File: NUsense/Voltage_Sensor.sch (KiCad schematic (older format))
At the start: 4 parts, among them U11? ACS724

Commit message: Change hierarchy layout
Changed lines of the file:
@@
 LIBS:valves
 LIBS:ADM6713RAKS
+LIBS:Header_Connectors
 LIBS:MPU6000
 LIBS:NUbots
 LIBS:STM32F746ZGT6
-LIBS:Header_Connectors
 LIBS:NUsense-cache
 EELAYER 25 0
@@
 Connection ~ 3750 1600
 Connection ~ 3450 1700
-Text GLabel 4150 1700 2    60   Input ~ 0
+Text HLabel 4150 1700 2    60   Output ~ 0
 I_OUT
 $EndSCHEMATC

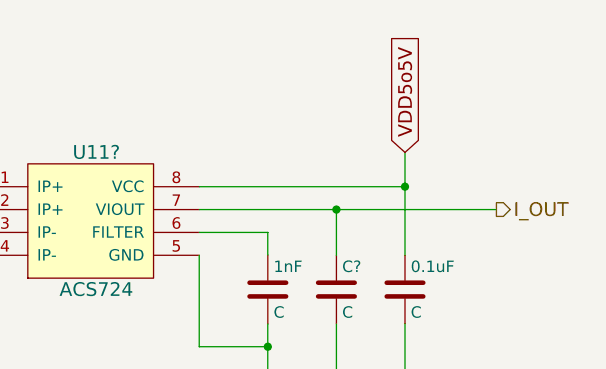
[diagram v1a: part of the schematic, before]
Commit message: Add power components
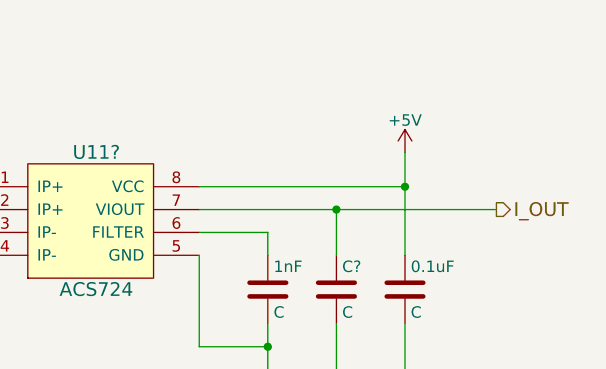
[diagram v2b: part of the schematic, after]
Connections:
- net VDD5o5V renamed +5V
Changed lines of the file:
@@
 	1600 1600 1900 1600
 Connection ~ 1800 1600
-Text GLabel 3750 1450 1    60   Input ~ 0
-VDD5o5V
 Connection ~ 3750 1600
 Connection ~ 3450 1700
 Text HLabel 4150 1700 2    60   Output ~ 0
 I_OUT
+$Comp
+L +5V #PWR?
+U 1 1 5A71C782
+P 3750 1450
+F 0 "#PWR?" H 3750 1300 50  0001 C CNN
+F 1 "+5V" H 3750 1590 50  0000 C CNN
+F 2 "" H 3750 1450 50  0001 C CNN
+F 3 "" H 3750 1450 50  0001 C CNN
+	1    3750 1450
+	1    0    0    -1
+$EndComp
 $EndSCHEMATC

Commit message: Correct Broken Files
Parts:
- added C? (x9): C, symbol C
- added R? (x7): R, symbol R
- added R?: R_Variable, symbol R_Variable
- added R?: 1M, symbol R
- added U?: bq76920, symbol bq76920
- added U?: 5_PIN_JST, symbol 5_PIN_JST
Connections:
- net GND: now also C?.2, C?.2, C?.2, C?.2, R?.1, R?.1, U?.3 (VSS)
- new net: C?.1, R?.1, U?.10 (BAT)
- new net: C?.1, C?.2, R?.1, R?.2, U?.12 (VC5), U?.9 (REGSRC)
- new net: C?.1, C?.2, R?.1, U?.13 (VC4), U?.14 (VC3)
- new net: C?.1, C?.2, R?.1, U?.15 (VC2)
- new net: C?.1, C?.2, R?.1, R?.1, U?.16 (VC1)
- new net: C?.1, R?.1, U?.17 (VC0)
- new net: R?.2, R?.2, U?.6 (TS1)
- new net: C?.1, U?.7 (CAP1)
- new net: C?.1, C?.2, R?.2, U?.1 (GND)
- new net: R?.2, U?.2 (V1)
- new net: R?.2, U?.3 (V2)
- new net: R?.2, U?.4 (V3)
- new net: R?.2, U?.5 (V4)
- new net +3V3: C?.1, U?.8 (REGOUT)
- new net VS_ALERT: R?.2, U?.20 (ALERT)
- new net VS_SCL: U?.5 (SCL)
- new net VS_SDA: U?.4 (SDA)

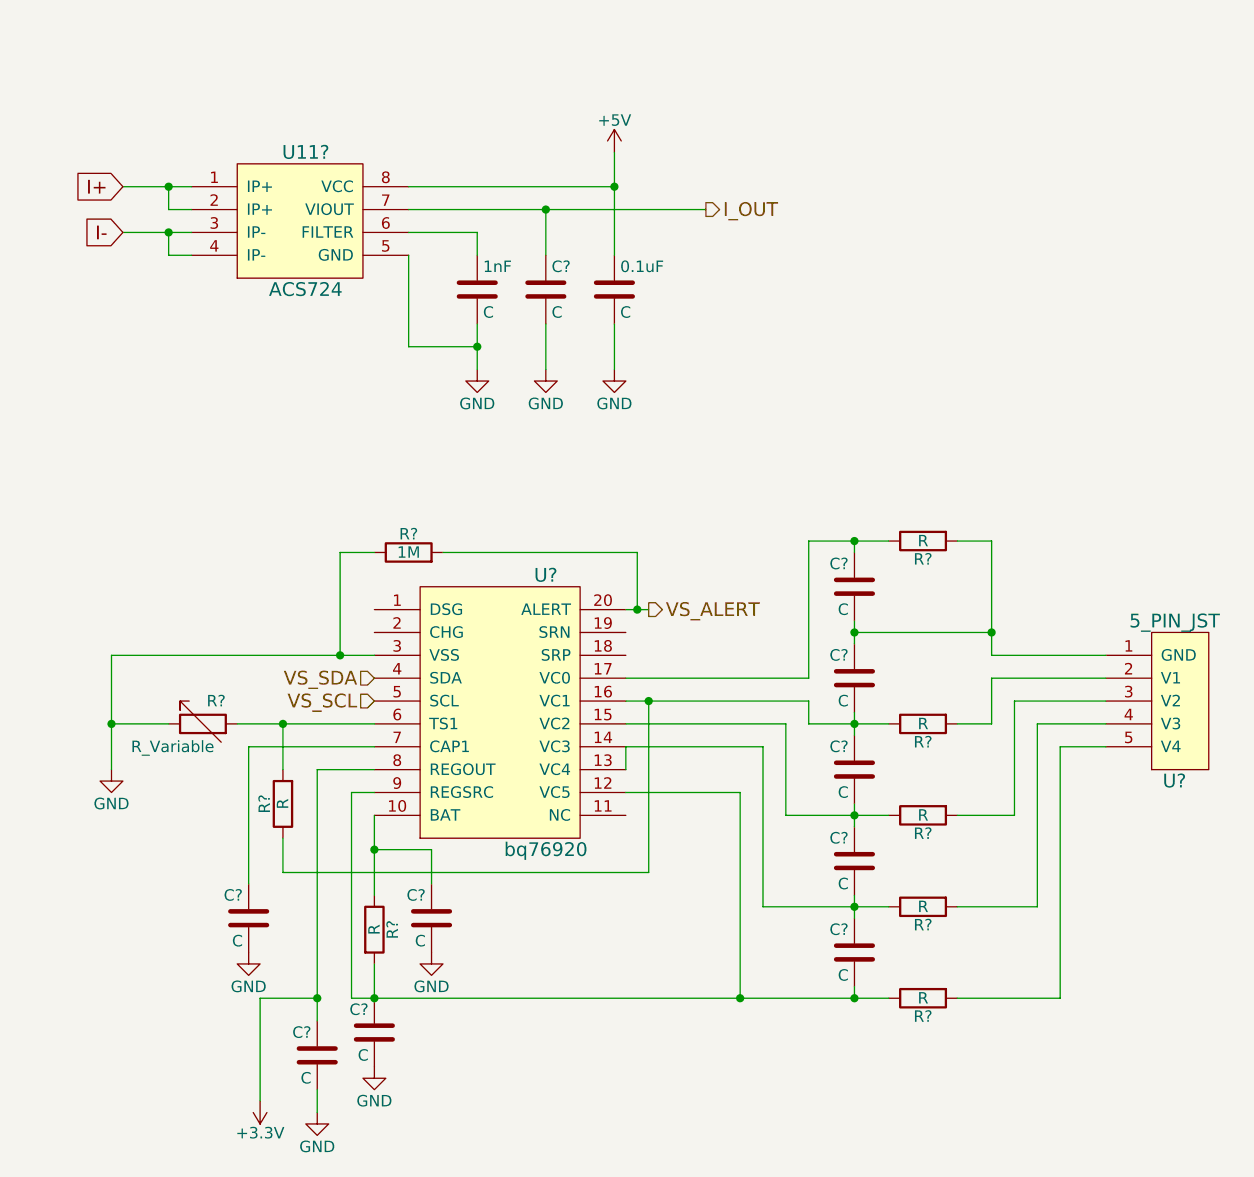
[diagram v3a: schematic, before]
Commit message: Adds annotations and footprints to all components
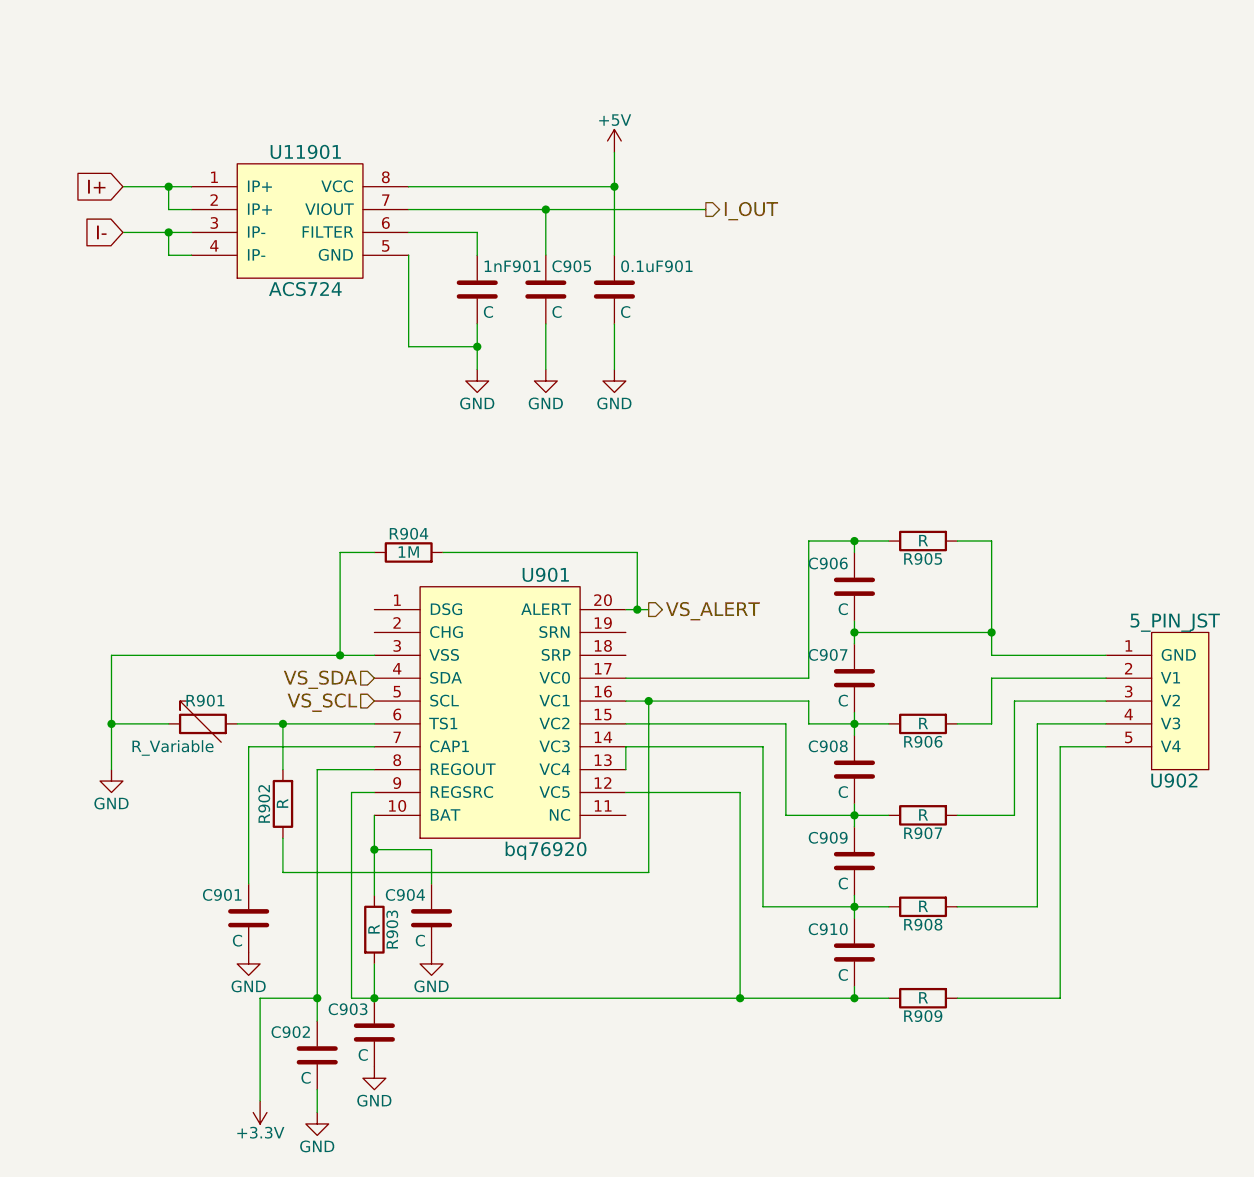
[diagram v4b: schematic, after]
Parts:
- 0.1uF901: renamed from 0.1uF; footprint (none) -> Capacitors_SMD:C_0805_HandSoldering
- 1nF901: renamed from 1nF; footprint (none) -> Capacitors_SMD:C_0805_HandSoldering
- C901, C902, C903, C904, C905, C906, C907, C908, C909, C910: renamed from C?; footprint (none) -> Capacitors_SMD:C_0805_HandSoldering
- R901, R902, R903, R904, R905, R906, R907, R908, R909: renamed from R?; footprint (none) -> Resistors_SMD:R_0805_HandSoldering
- U11901: renamed from U11?; footprint (none) -> Footprints:SOIC-8
- U901: renamed from U?; footprint (none) -> Footprints:SOIC-20
- gave numbers to parts that had none: 1

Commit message: More Changes
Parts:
- 0.1uF701: renamed from 0.1uF901; value C -> 0.1nF
- 1nF701: renamed from 1nF901; value C -> 1nF
- renumbered C901 to C701, C902 to C702, C903 to C703, C904 to C704, C905 to C705, C906 to C706, C907 to C707, C908 to C708, C909 to C709, C910 to C710, R901 to R701, R902 to R702, R903 to R703, R904 to R704, R905 to R705, R906 to R706, R907 to R707, R908 to R708, R909 to R709, U11901 to U701, U901 to U702, U902 to U703
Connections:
- net I+ renamed BATT_+
- net I- renamed BATT_-
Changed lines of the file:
@@
 $Descr A4 11693 8268
 encoding utf-8
-Sheet 9 12
+Sheet 7 12
 Title ""
 Date ""
@@
 $EndDescr
 $Comp
-L ACS724 U11901
+L ACS724 U701
 U 1 1 5A6D62FA
 P 2100 2000
-F 0 "U11901" H 2400 2550 60  0000 C CNN
+F 0 "U701" H 2400 2550 60  0000 C CNN
 F 1 "ACS724" H 2400 1950 60  0000 C CNN
 F 2 "Footprints:SOIC-8" H 2100 2000 60  0001 C CNN
@@
 $EndComp
 $Comp
-L C 1nF901
+L C 1nF701
 U 1 1 5A6D635A
 P 3150 2050
-F 0 "1nF901" H 3175 2150 50  0000 L CNN
-F 1 "C" H 3175 1950 50  0000 L CNN
+F 0 "1nF701" H 3175 2150 50  0000 L CNN
+F 1 "1nF" H 3175 1950 50  0000 L CNN
 F 2 "Capacitors_SMD:C_0805_HandSoldering" H 3188 1900 50  0001 C CNN
 F 3 "" H 3150 2050 50  0001 C CNN
@@
 $EndComp
 $Comp
-L C C905
+L C C705
 U 1 1 5A6D63B5
 P 3450 2050
-F 0 "C905" H 3475 2150 50  0000 L CNN
+F 0 "C705" H 3475 2150 50  0000 L CNN
 F 1 "C" H 3475 1950 50  0000 L CNN
 F 2 "Capacitors_SMD:C_0805_HandSoldering" H 3488 1900 50  0001 C CNN
@@
 $EndComp
 $Comp
-L C 0.1uF901
+L C 0.1uF701
 U 1 1 5A6D63DA
 P 3750 2050
-F 0 "0.1uF901" H 3775 2150 50  0000 L CNN
-F 1 "C" H 3775 1950 50  0000 L CNN
+F 0 "0.1uF701" H 3775 2150 50  0000 L CNN
+F 1 "0.1nF" H 3775 1950 50  0000 L CNN
 F 2 "Capacitors_SMD:C_0805_HandSoldering" H 3788 1900 50  0001 C CNN
 F 3 "" H 3750 2050 50  0001 C CNN
@@
 $EndComp
 $Comp
-L GND #PWR907
+L GND #PWR067
 U 1 1 5A6D644B
 P 3150 2400
-F 0 "#PWR907" H 3150 2150 50  0001 C CNN
+F 0 "#PWR067" H 3150 2150 50  0001 C CNN
 F 1 "GND" H 3150 2250 50  0000 C CNN
 F 2 "" H 3150 2400 50  0001 C CNN
@@
 $EndComp
 $Comp
-L GND #PWR908
+L GND #PWR068
 U 1 1 5A6D6469
 P 3450 2400
-F 0 "#PWR908" H 3450 2150 50  0001 C CNN
+F 0 "#PWR068" H 3450 2150 50  0001 C CNN
 F 1 "GND" H 3450 2250 50  0000 C CNN
 F 2 "" H 3450 2400 50  0001 C CNN
@@
 $EndComp
 $Comp
-L GND #PWR910
+L GND #PWR069
 U 1 1 5A6D6480
 P 3750 2400
-F 0 "#PWR910" H 3750 2150 50  0001 C CNN
+F 0 "#PWR069" H 3750 2150 50  0001 C CNN
 F 1 "GND" H 3750 2250 50  0000 C CNN
 F 2 "" H 3750 2400 50  0001 C CNN
@@
 	1    0    0    -1
 $EndComp
-Text GLabel 1600 1600 0    60   Input ~ 0
-I+
-Text GLabel 1600 1800 0    60   Input ~ 0
-I-
 Text HLabel 4150 1700 2    60   Output ~ 0
 I_OUT
 $Comp
-L +5V #PWR909
+L +5V #PWR070
 U 1 1 5A71C782
 P 3750 1450
-F 0 "#PWR909" H 3750 1300 50  0001 C CNN
+F 0 "#PWR070" H 3750 1300 50  0001 C CNN
 F 1 "+5V" H 3750 1590 50  0000 C CNN
 F 2 "" H 3750 1450 50  0001 C CNN
@@
 $EndComp
 $Comp
-L bq76920 U901
+L bq76920 U702
 U 1 1 5A7144DD
 P 2900 4450
-F 0 "U901" H 3450 5600 60  0000 C CNN
+F 0 "U702" H 3450 5600 60  0000 C CNN
 F 1 "bq76920" H 3450 4400 60  0000 C CNN
 F 2 "Footprints:SOIC-20" H 2900 4450 60  0001 C CNN
@@
 $EndComp
 $Comp
-L 5_PIN_JST U902
+L 5_PIN_JST U703
 U 1 1 5A71501A
 P 6350 3550
-F 0 "U902" H 6500 4200 60  0000 C CNN
+F 0 "U703" H 6500 4200 60  0000 C CNN
 F 1 "5_PIN_JST" H 6500 3500 60  0000 C CNN
 F 2 "" H 6350 3550 60  0001 C CNN
@@
 $EndComp
 $Comp
-L R R907
+L R R707
 U 1 1 5A7150F8
 P 5100 4350
-F 0 "R907" V 5180 4350 50  0000 C CNN
+F 0 "R707" V 5180 4350 50  0000 C CNN
 F 1 "R" V 5100 4350 50  0000 C CNN
 F 2 "Resistors_SMD:R_0805_HandSoldering" V 5030 4350 50  0001 C CNN
@@
 $EndComp
 $Comp
-L R R905
+L R R705
 U 1 1 5A71513F
 P 5100 3150
-F 0 "R905" V 5180 3150 50  0000 C CNN
+F 0 "R705" V 5180 3150 50  0000 C CNN
 F 1 "R" V 5100 3150 50  0000 C CNN
 F 2 "Resistors_SMD:R_0805_HandSoldering" V 5030 3150 50  0001 C CNN
@@
 $EndComp
 $Comp
-L R R906
+L R R706
 U 1 1 5A71518D
 P 5100 3950
-F 0 "R906" V 5180 3950 50  0000 C CNN
+F 0 "R706" V 5180 3950 50  0000 C CNN
 F 1 "R" V 5100 3950 50  0000 C CNN
 F 2 "Resistors_SMD:R_0805_HandSoldering" V 5030 3950 50  0001 C CNN
@@
 $EndComp
 $Comp
-L C C907
+L C C707
 U 1 1 5A71527F
 P 4800 3750
-F 0 "C907" H 4825 3850 50  0000 L CNN
+F 0 "C707" H 4825 3850 50  0000 L CNN
 F 1 "C" H 4825 3650 50  0000 L CNN
 F 2 "Capacitors_SMD:C_0805_HandSoldering" H 4838 3600 50  0001 C CNN
@@
 $EndComp
 $Comp
-L C C908
+L C C708
 U 1 1 5A715314
 P 4800 4150
-F 0 "C908" H 4825 4250 50  0000 L CNN
+F 0 "C708" H 4825 4250 50  0000 L CNN
 F 1 "C" H 4825 4050 50  0000 L CNN
 F 2 "Capacitors_SMD:C_0805_HandSoldering" H 4838 4000 50  0001 C CNN
@@
 $EndComp
 $Comp
-L R R908
+L R R708
 U 1 1 5A7153F1
 P 5100 4750
-F 0 "R908" V 5180 4750 50  0000 C CNN
+F 0 "R708" V 5180 4750 50  0000 C CNN
 F 1 "R" V 5100 4750 50  0000 C CNN
 F 2 "Resistors_SMD:R_0805_HandSoldering" V 5030 4750 50  0001 C CNN
@@
 $EndComp
 $Comp
-L C C909
+L C C709
 U 1 1 5A7153F7
 P 4800 4550
-F 0 "C909" H 4825 4650 50  0000 L CNN
+F 0 "C709" H 4825 4650 50  0000 L CNN
 F 1 "C" H 4825 4450 50  0000 L CNN
 F 2 "Capacitors_SMD:C_0805_HandSoldering" H 4838 4400 50  0001 C CNN
@@
 $EndComp
 $Comp
-L R R909
+L R R709
 U 1 1 5A715441
 P 5100 5150
-F 0 "R909" V 5180 5150 50  0000 C CNN
+F 0 "R709" V 5180 5150 50  0000 C CNN
 F 1 "R" V 5100 5150 50  0000 C CNN
 F 2 "Resistors_SMD:R_0805_HandSoldering" V 5030 5150 50  0001 C CNN
@@
 $EndComp
 $Comp
-L C C910
+L C C710
 U 1 1 5A715447
 P 4800 4950
-F 0 "C910" H 4825 5050 50  0000 L CNN
+F 0 "C710" H 4825 5050 50  0000 L CNN
 F 1 "C" H 4825 4850 50  0000 L CNN
 F 2 "Capacitors_SMD:C_0805_HandSoldering" H 4838 4800 50  0001 C CNN
@@
 $EndComp
 $Comp
-L C C906
+L C C706
 U 1 1 5A715642
 P 4800 3350
-F 0 "C906" H 4825 3450 50  0000 L CNN
+F 0 "C706" H 4825 3450 50  0000 L CNN
 F 1 "C" H 4825 3250 50  0000 L CNN
 F 2 "Capacitors_SMD:C_0805_HandSoldering" H 4838 3200 50  0001 C CNN
@@
 VS_SDA
 $Comp
-L R R902
+L R R702
 U 1 1 5A717567
 P 2300 4300
-F 0 "R902" V 2380 4300 50  0000 C CNN
+F 0 "R702" V 2380 4300 50  0000 C CNN
 F 1 "R" V 2300 4300 50  0000 C CNN
 F 2 "Resistors_SMD:R_0805_HandSoldering" V 2230 4300 50  0001 C CNN
@@
 $EndComp
 $Comp
-L R_Variable R901
+L R_Variable R701
 U 1 1 5A7175C4
 P 1950 3950
-F 0 "R901" V 2050 3850 50  0000 L CNN
+F 0 "R701" V 2050 3850 50  0000 L CNN
 F 1 "R_Variable" V 1850 3900 50  0000 L CNN
 F 2 "Resistors_SMD:R_0805_HandSoldering" V 1880 3950 50  0001 C CNN
@@
 $EndComp
 $Comp
-L GND #PWR901
+L GND #PWR071
 U 1 1 5A7178EF
 P 1550 4150
-F 0 "#PWR901" H 1550 3900 50  0001 C CNN
+F 0 "#PWR071" H 1550 3900 50  0001 C CNN
 F 1 "GND" H 1550 4000 50  0000 C CNN
 F 2 "" H 1550 4150 50  0001 C CNN
@@
 VS_ALERT
 $Comp
-L C C902
+L C C702
 U 1 1 5A718214
 P 2450 5400
-F 0 "C902" H 2475 5500 50  0000 L CNN
+F 0 "C702" H 2475 5500 50  0000 L CNN
 F 1 "C" H 2475 5300 50  0000 L CNN
 F 2 "Capacitors_SMD:C_0805_HandSoldering" H 2488 5250 50  0001 C CNN
@@
 $EndComp
 $Comp
-L GND #PWR904
+L GND #PWR072
 U 1 1 5A7183EF
 P 2450 5650
-F 0 "#PWR904" H 2450 5400 50  0001 C CNN
+F 0 "#PWR072" H 2450 5400 50  0001 C CNN
 F 1 "GND" H 2450 5500 50  0000 C CNN
 F 2 "" H 2450 5650 50  0001 C CNN
@@
 Connection ~ 2450 5150
 $Comp
-L R R903
+L R R703
 U 1 1 5A7187DD
 P 2700 4850
-F 0 "R903" V 2780 4850 50  0000 C CNN
+F 0 "R703" V 2780 4850 50  0000 C CNN
 F 1 "R" V 2700 4850 50  0000 C CNN
 F 2 "Resistors_SMD:R_0805_HandSoldering" V 2630 4850 50  0001 C CNN
@@
 Connection ~ 2700 5150
 $Comp
-L GND #PWR906
+L GND #PWR073
 U 1 1 5A7189F4
 P 2950 4950
-F 0 "#PWR906" H 2950 4700 50  0001 C CNN
+F 0 "#PWR073" H 2950 4700 50  0001 C CNN
 F 1 "GND" H 2950 4800 50  0000 C CNN
 F 2 "" H 2950 4950 50  0001 C CNN
@@
 $EndComp
 $Comp
-L C C904
+L C C704
 U 1 1 5A718B0F
 P 2950 4800
-F 0 "C904" H 2975 4900 50  0000 L CNN
+F 0 "C704" H 2975 4900 50  0000 L CNN
 F 1 "C" H 2975 4700 50  0000 L CNN
 F 2 "Capacitors_SMD:C_0805_HandSoldering" H 2988 4650 50  0001 C CNN
@@
 	2150 4050 2150 4650
 $Comp
-L C C901
+L C C701
 U 1 1 5A718C78
 P 2150 4800
-F 0 "C901" H 2175 4900 50  0000 L CNN
+F 0 "C701" H 2175 4900 50  0000 L CNN
 F 1 "C" H 2175 4700 50  0000 L CNN
 F 2 "Capacitors_SMD:C_0805_HandSoldering" H 2188 4650 50  0001 C CNN
@@
 $EndComp
 $Comp
-L GND #PWR902
+L GND #PWR074
 U 1 1 5A718CD0
 P 2150 4950
-F 0 "#PWR902" H 2150 4700 50  0001 C CNN
+F 0 "#PWR074" H 2150 4700 50  0001 C CNN
 F 1 "GND" H 2150 4800 50  0000 C CNN
 F 2 "" H 2150 4950 50  0001 C CNN
@@
 $EndComp
 $Comp
-L C C903
+L C C703
 U 1 1 5A719665
 P 2700 5300
-F 0 "C903" H 2725 5400 50  0000 L CNN
+F 0 "C703" H 2725 5400 50  0000 L CNN
 F 1 "C" H 2725 5200 50  0000 L CNN
 F 2 "Capacitors_SMD:C_0805_HandSoldering" H 2738 5150 50  0001 C CNN
@@
 $EndComp
 $Comp
-L GND #PWR905
+L GND #PWR075
 U 1 1 5A7196C4
 P 2700 5450
-F 0 "#PWR905" H 2700 5200 50  0001 C CNN
+F 0 "#PWR075" H 2700 5200 50  0001 C CNN
 F 1 "GND" H 2700 5300 50  0000 C CNN
 F 2 "" H 2700 5450 50  0001 C CNN
@@
 $EndComp
 $Comp
-L +3.3V #PWR903
+L +3.3V #PWR076
 U 1 1 5A719D8E
 P 2200 5600
-F 0 "#PWR903" H 2200 5450 50  0001 C CNN
+F 0 "#PWR076" H 2200 5450 50  0001 C CNN
 F 1 "+3.3V" H 2200 5740 50  0000 C CNN
 F 2 "" H 2200 5600 50  0001 C CNN
@@
 Connection ~ 3850 3450
 $Comp
-L R R904
+L R R704
 U 1 1 5A71C3E9
 P 2850 3200
-F 0 "R904" V 2930 3200 50  0000 C CNN
+F 0 "R704" V 2930 3200 50  0000 C CNN
 F 1 "1M" V 2850 3200 50  0000 C CNN
 F 2 "Resistors_SMD:R_0805_HandSoldering" V 2780 3200 50  0001 C CNN
@@
 Wire Wire Line
 	3850 3200 3000 3200
+Text HLabel 1600 1600 0    60   BiDi ~ 0
+BATT_+
+Text HLabel 1600 1800 0    60   BiDi ~ 0
+BATT_-
 $EndSCHEMATC
